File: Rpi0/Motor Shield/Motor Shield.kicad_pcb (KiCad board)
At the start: 2 copper layers, 1 part, among them U1 IFX9201

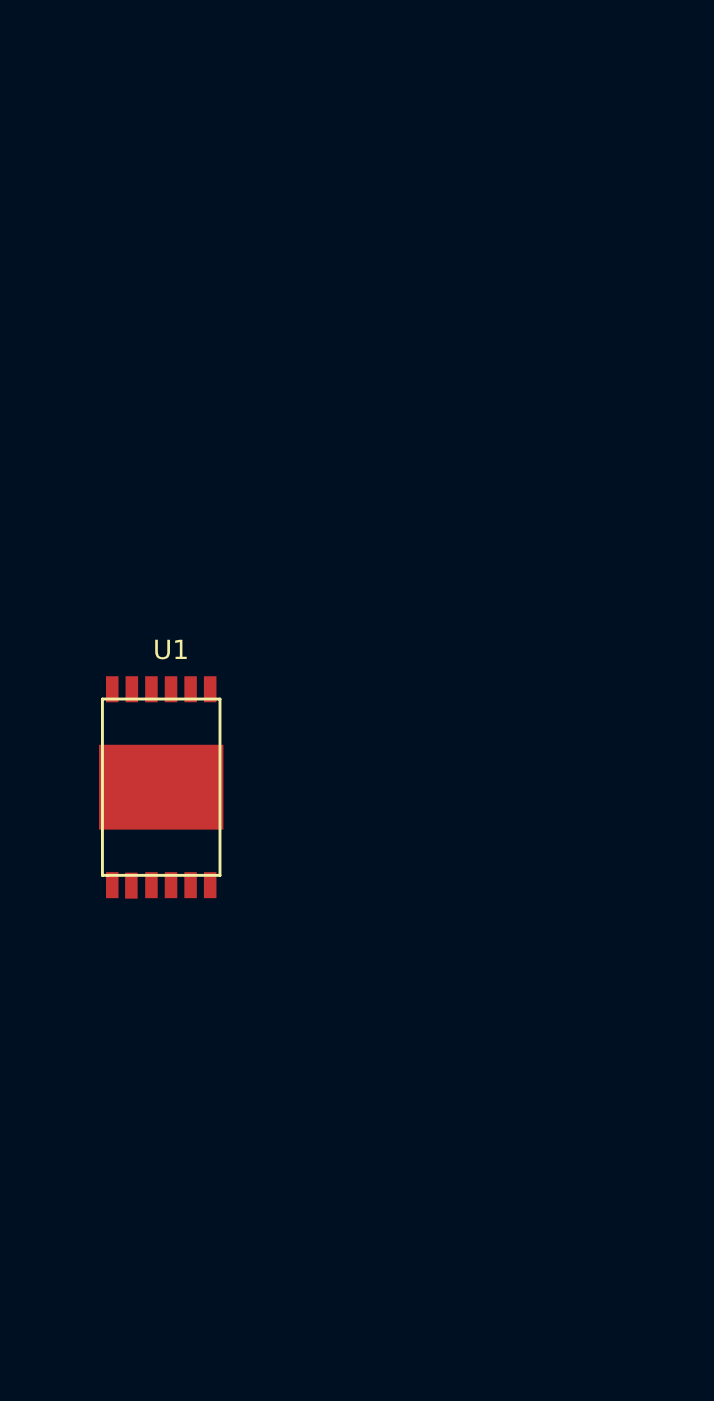
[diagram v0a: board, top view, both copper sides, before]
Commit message: [RPI0] [Motor Shield] Almost finished version, need to trace
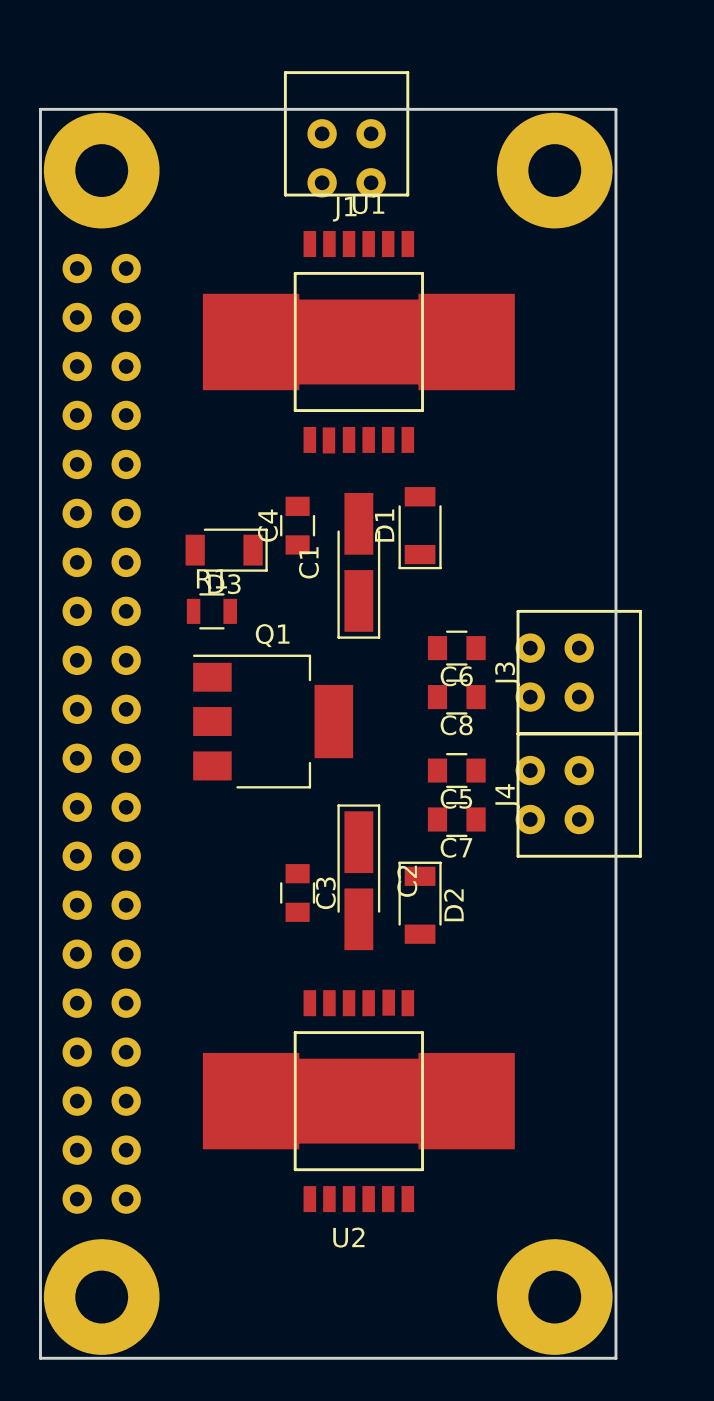
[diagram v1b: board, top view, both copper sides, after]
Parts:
- added C1: 100uF, Capacitors_Tantalum_SMD:CP_Tantalum_Case-A_EIA-3216-18_Hand, F.Cu at (158.8, 93.3)
- added C2: 100uF, Capacitors_Tantalum_SMD:CP_Tantalum_Case-A_EIA-3216-18_Hand, F.Cu at (158.8, 109.9)
- added C3: 100nF, Capacitors_SMD:C_0805, F.Cu at (155.6, 110.5)
- added C4: 100nF, Capacitors_SMD:C_0805, F.Cu at (155.6, 91.4)
- added C5: 10nF, Capacitors_SMD:C_0805, F.Cu at (163.8, 104.1)
- added C6: 10nF, Capacitors_SMD:C_0805, F.Cu at (163.8, 97.8)
- added C7: 10nF, Capacitors_SMD:C_0805, F.Cu at (163.8, 106.7)
- added C8: 10nF, Capacitors_SMD:C_0805, F.Cu at (163.8, 100.3)
- added D1: < 40V, Diodes_SMD:D_1206, F.Cu at (161.9, 91.4)
- added D2: < 40V, Diodes_SMD:D_1206, F.Cu at (161.9, 111.1)
- added D3: 10V, Diodes_SMD:D_1206, F.Cu at (151.8, 92.7)
- added J1: Conn_01x02, Rob:PCB_Terminal_1725656, F.Cu at (158.1, 71.1)
- added J2: Conn_02x20_Odd_Even, Rob:RPi0_Template, B.Cu at (152.4, 99.7)
- added J3: Conn_01x02, Rob:PCB_Terminal_1725656, F.Cu at (170.2, 99.1)
- added J4: Conn_01x02, Rob:PCB_Terminal_1725656, F.Cu at (170.2, 105.4)
- added Q1: Q_PMOS_GDSD, TO_SOT_Packages_SMD:SOT-223, F.Cu at (154.3, 101.6)
- added R1: 10k, Resistors_SMD:R_0805, F.Cu at (151.1, 95.9)
- added U2: IFX9201, Rob:IFX9201, F.Cu at (158.8, 121.3)
- moved U1 25.3 mm to (158.8, 81.9)
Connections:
- net Net-(U1-Pad1) renamed DIR1
- net Net-(U1-Pad11) renamed EN1
- net Net-(U1-Pad12) renamed PWM1
- U1 pad 10: Net-(U1-Pad10) -> BAT-
- U1 pad 2: Net-(U1-Pad2) -> BAT-
- U1 pad 3: Net-(U1-Pad3) -> +3V3
- U1 pad 4: Net-(U1-Pad4) -> BAT-PROT+
- U1 pad 5: Net-(U1-Pad5) -> OUT1
- U1 pad 6: Net-(U1-Pad6) -> BAT-
- U1 pad 7: Net-(U1-Pad7) -> OUT2
- U1 pad 8: Net-(U1-Pad8) -> BAT-
- U1 pad 9: Net-(U1-Pad9) -> BAT-
- U1 pad ~: Net-(U1-Pad~) -> BAT-
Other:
- board outline added: 29.8 x 64.8 mm

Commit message: Motor shield traced and finished
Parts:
- removed J2: Conn_02x20_Odd_Even, Rob:RPi0_Template
- added C10: 10uF, Capacitors_SMD:C_0805, F.Cu at (151.8, 95.9)
- added C11: 1uF, Capacitors_SMD:C_0805, F.Cu at (153.2, 85.3)
- added C12: 1uF, Capacitors_SMD:C_0805, F.Cu at (150.4, 87.1)
- added C13: 1uF, Capacitors_SMD:C_0805, F.Cu at (150.4, 90.9)
- added C14: 1uF, Capacitors_SMD:C_0805, F.Cu at (157.2, 85.6)
- added C9: 100nF, Capacitors_SMD:C_0805, F.Cu at (152.4, 107.3)
- added U3: LD1117S18TR_SOT223, TO_SOT_Packages_SMD:SOT-223-3_TabPin2, F.Cu at (154.9, 101.6)
- added U4: RPi0, Rob:RPi0_Template, B.Cu at (152.4, 99.7)
- added U5: LP5569, Housings_DFN_QFN:QFN-24-1EP_4x4mm_Pitch0.5mm, F.Cu at (155.4, 89.7)
- moved Q1 24.8 mm to (153.0, 76.8)
- moved R1 24.1 mm to (151.1, 71.8)
- moved D3 10.8 mm to (151.1, 81.9), turned to 0 degrees
- moved C7 6.35 mm to (163.8, 100.3)
- moved C8 6.35 mm to (163.8, 106.7)
- moved C5 6.35 mm to (163.8, 97.8)
- moved C6 6.35 mm to (163.8, 104.1)
- moved J3 6.35 mm to (170.2, 105.4)
- moved J4 6.35 mm to (170.2, 99.1)
- moved C3 5.80 mm to (161.3, 111.5)
- moved C4 5.61 mm to (161.0, 92.7)
- moved C2 5.43 mm to (163.8, 111.8)
- moved D1 5.36 mm to (167.1, 92.7)
- moved U2 5.24 mm to (163.8, 122.6)
- moved C1 5.12 mm to (163.8, 92.7)
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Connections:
- U1 pad 2: BAT- -> +3V3
- U1 pad 3: +3V3 -> ERROR1
- U2 pad 2: BAT- -> +3V3
- U2 pad 3: +3V3 -> ERROR2
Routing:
- net BAT-: track 0.00 -> 92.5 mm, vias 0 -> 13
- net +3V3: track 0.00 -> 92.3 mm, vias 0 -> 5
- net BAT-PROT+: track 0.00 -> 75.1 mm, vias 0 -> 4
- net EN2: track 0.00 -> 54.5 mm, vias 0 -> 1
- net PWM2: track 0.00 -> 50.3 mm, vias 0 -> 2
- net OUT4: track 0.00 -> 43.9 mm, vias 0 -> 2
- net DIR2: track 0.00 -> 41.4 mm, vias 0 -> 1
- net EN1: track 0.00 -> 36.5 mm, vias 0 -> 1
- net OUT2: track 0.00 -> 28.1 mm, vias 0 -> 2
- net DIR1: track 0.00 -> 26.3 mm
- net LV: track 0.00 -> 23.9 mm, vias 0 -> 2
- net SDA: track 0.00 -> 23.4 mm
- net OUT1: track 0.00 -> 22.3 mm, vias 0 -> 2
- net OUT3: track 0.00 -> 18.7 mm, vias 0 -> 2
- net SCL: track 0.00 -> 17.3 mm
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- added copper zone on B.Cu, net BAT-
- added copper zone on F.Cu, net BAT-

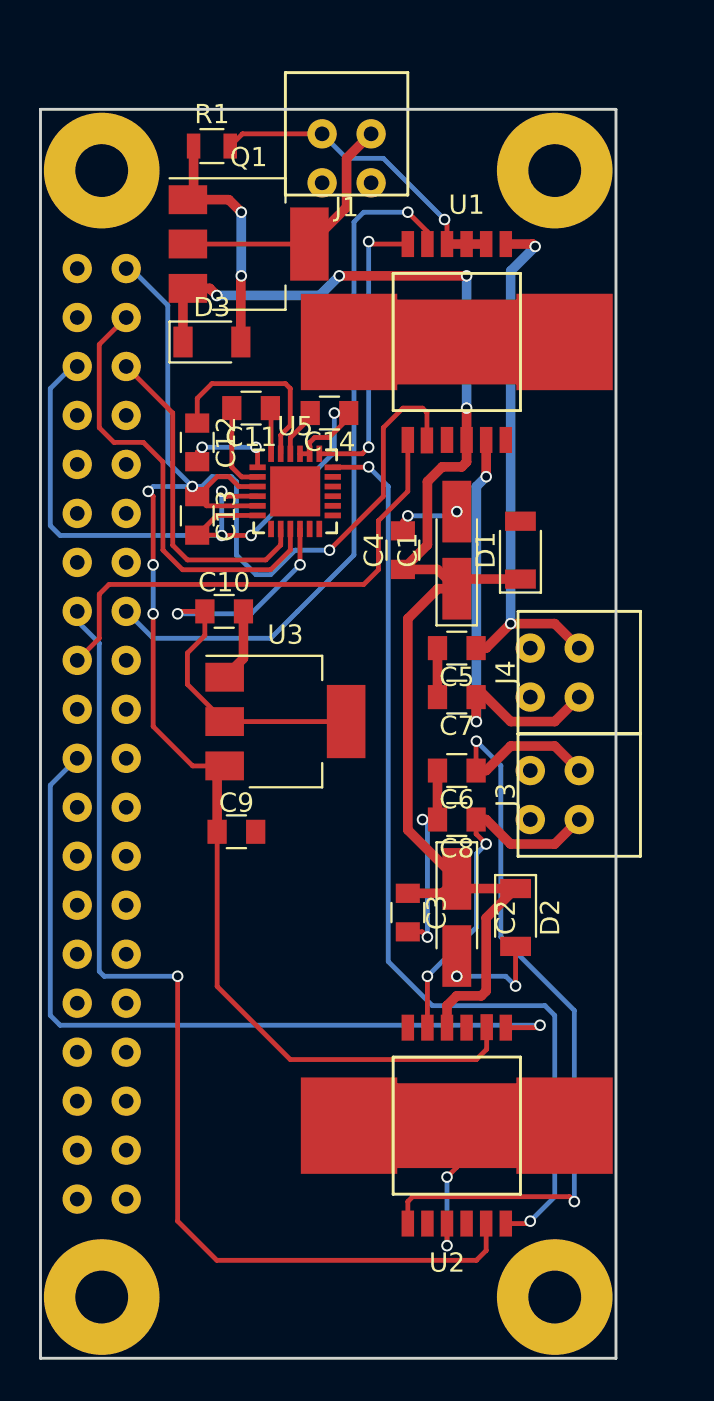
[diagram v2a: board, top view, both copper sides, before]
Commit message: Changed TL5569 to PIC16F1509
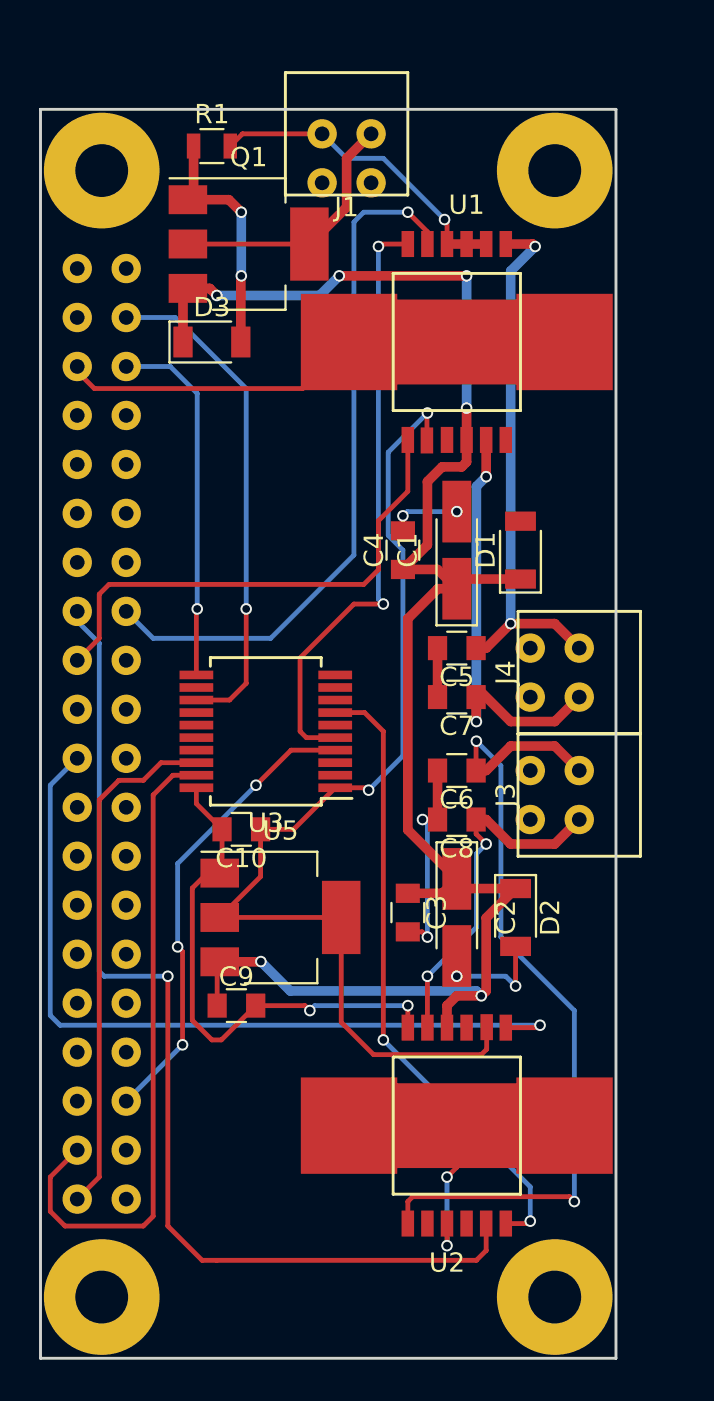
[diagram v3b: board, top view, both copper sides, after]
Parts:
- removed C11, C12, C13, C14: 1uF, Capacitors_SMD:C_0805
- U3: value LD1117S18TR_SOT223 -> PIC16(L)F1509-I/SO; footprint TO_SOT_Packages_SMD:SOT-223-3_TabPin2 -> Housings_SSOP:SSOP-20_5.3x7.2mm_Pitch0.65mm
- U5: value LP5569 -> LD1117S33TR_SOT223; footprint Housings_DFN_QFN:QFN-24-1EP_4x4mm_Pitch0.5mm -> TO_SOT_Packages_SMD:SOT-223-3_TabPin2
- moved U5 22.1 mm to (154.7, 111.8)
- moved C10 11.3 mm to (152.7, 107.2), turned to 180 degrees
- moved C9 9.02 mm to (152.4, 116.3)
- moved U3 1.14 mm to (153.9, 102.1), turned to 180 degrees
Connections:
- C10 pad 1: LV -> +3V3
- C9 pad 1: +3V3 -> BAT-PROT+
- U3 pad 1: BAT- -> +3V3
- U3 pad 2: LV -> Net-(U3-Pad2)
- U3 pad 3: +3V3 -> Net-(U3-Pad3)
- U4 pad 1: +3V3 -> Net-(U4-Pad1)
- U4 pad 35: Net-(U4-Pad35) -> MCLR
- U4 pad 38: Net-(U4-Pad38) -> ICSP_DAT
- U4 pad 40: Net-(U4-Pad40) -> ICSP_CLK
- U5 pad 1: Net-(C12-Pad2) -> BAT-
- U5 pad 2: Net-(C11-Pad2) -> +3V3
- U5 pad 3: +3V3 -> BAT-PROT+
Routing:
- net +3V3: track 92.3 -> 56.1 mm, vias 5 -> 2
- net ICSP_DAT: track 0.00 -> 34.1 mm
- net ICSP_CLK: track 0.00 -> 27.0 mm
- net MCLR: track 0.00 -> 24.2 mm, vias 0 -> 3
- net LV: track 23.9 -> 0.00 mm, vias 2 -> 0
- net PWM2: track 50.3 -> 32.8 mm
- net BAT-PROT+: track 75.1 -> 91.7 mm, vias 4 -> 6
- net PWM1: track 15.5 -> 31.5 mm
- net Net-(C12-Pad1): track 10.1 -> 0.00 mm
- net Net-(C12-Pad2): track 4.72 -> 0.00 mm, vias 2 -> 0
- net Net-(C11-Pad2): track 4.61 -> 0.00 mm
- net SDA: track 23.4 -> 26.0 mm, vias 0 -> 1
- net Net-(C11-Pad1): track 2.43 -> 0.00 mm
- net Net-(C14-Pad2): track 2.29 -> 0.00 mm
- net BAT-: track 92.5 -> 90.6 mm, vias 13 -> 11
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
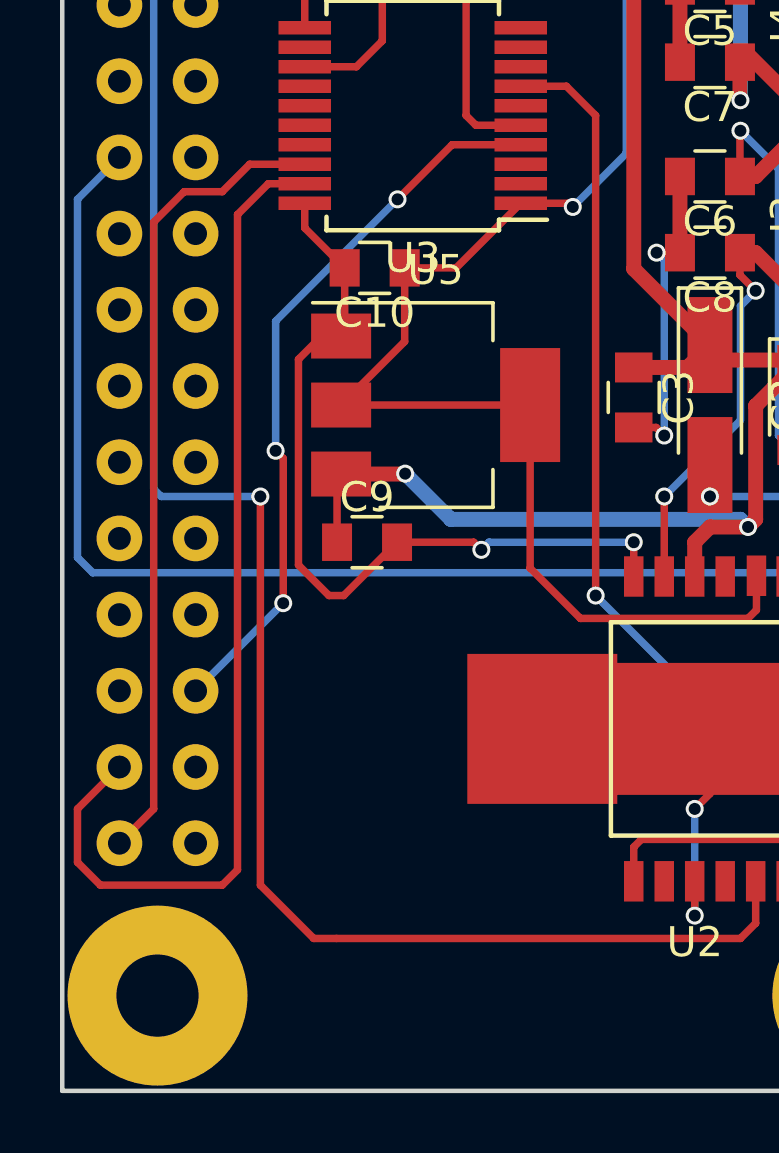
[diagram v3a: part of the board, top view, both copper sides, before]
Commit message: Added ICSP to microchip pic
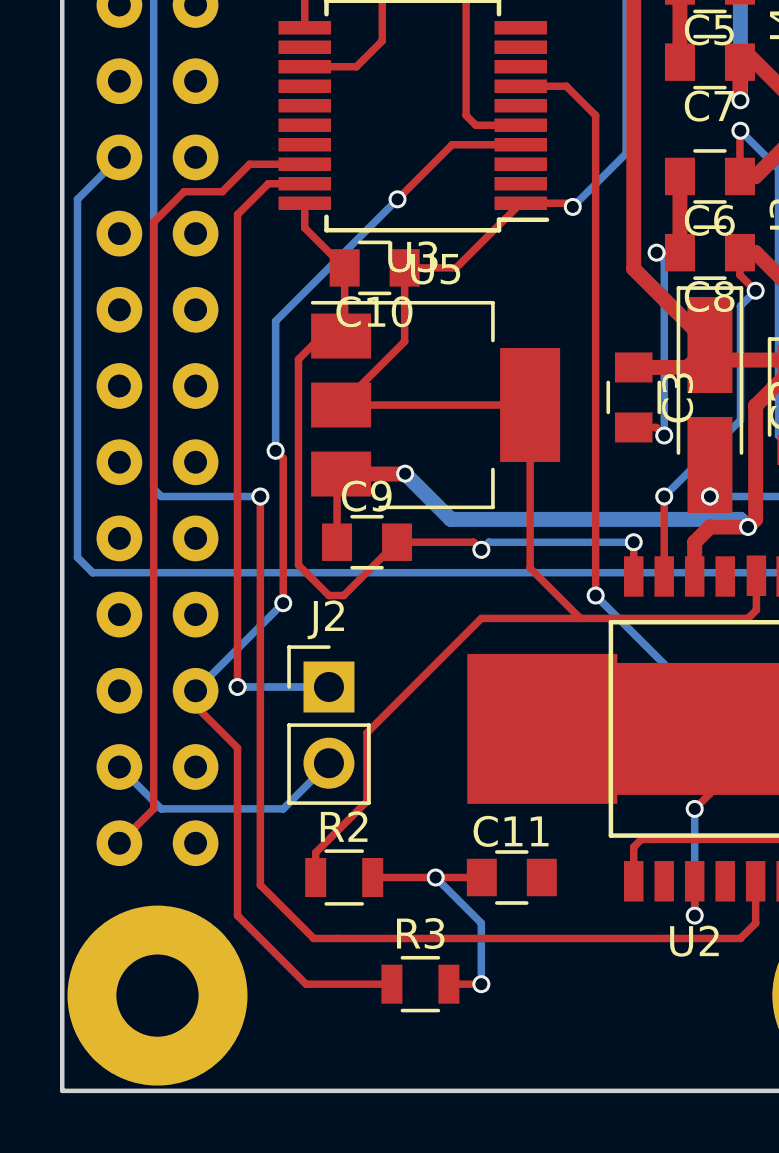
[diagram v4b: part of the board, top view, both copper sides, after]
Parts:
- added C11: 1uF, Capacitors_SMD:C_0805, F.Cu at (157.2, 127.5)
- added J2: Conn_01x02, Pin_Headers:Pin_Header_Straight_1x02_Pitch2.54mm, F.Cu at (151.1, 121.2)
- added R2: 10k, Resistors_SMD:R_0805, F.Cu at (151.6, 127.5)
- added R3: 470, Resistors_SMD:R_0805, F.Cu at (154.2, 131.1)
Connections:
- U3 pad 19: ICSP_DAT -> Net-(J2-Pad1)
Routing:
- net ICSP_DAT: track 34.1 -> 8.19 mm
- net Net-(J2-Pad1): track 0.00 -> 21.5 mm, vias 0 -> 1
- net +3V3: track 56.1 -> 70.3 mm
- net MCLR: track 24.2 -> 38.4 mm
- net Net-(C11-Pad1): track 0.00 -> 8.91 mm, vias 0 -> 2
